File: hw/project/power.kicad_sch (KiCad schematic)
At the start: 27 parts, among them Q1 MOSFET, N-CH, SINGLE, 120A, 6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, Q2 MOSFET, N-CH, SINGLE, 120A, 6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, U3 LM74502DDFR, U4 LMR51610XDBVR

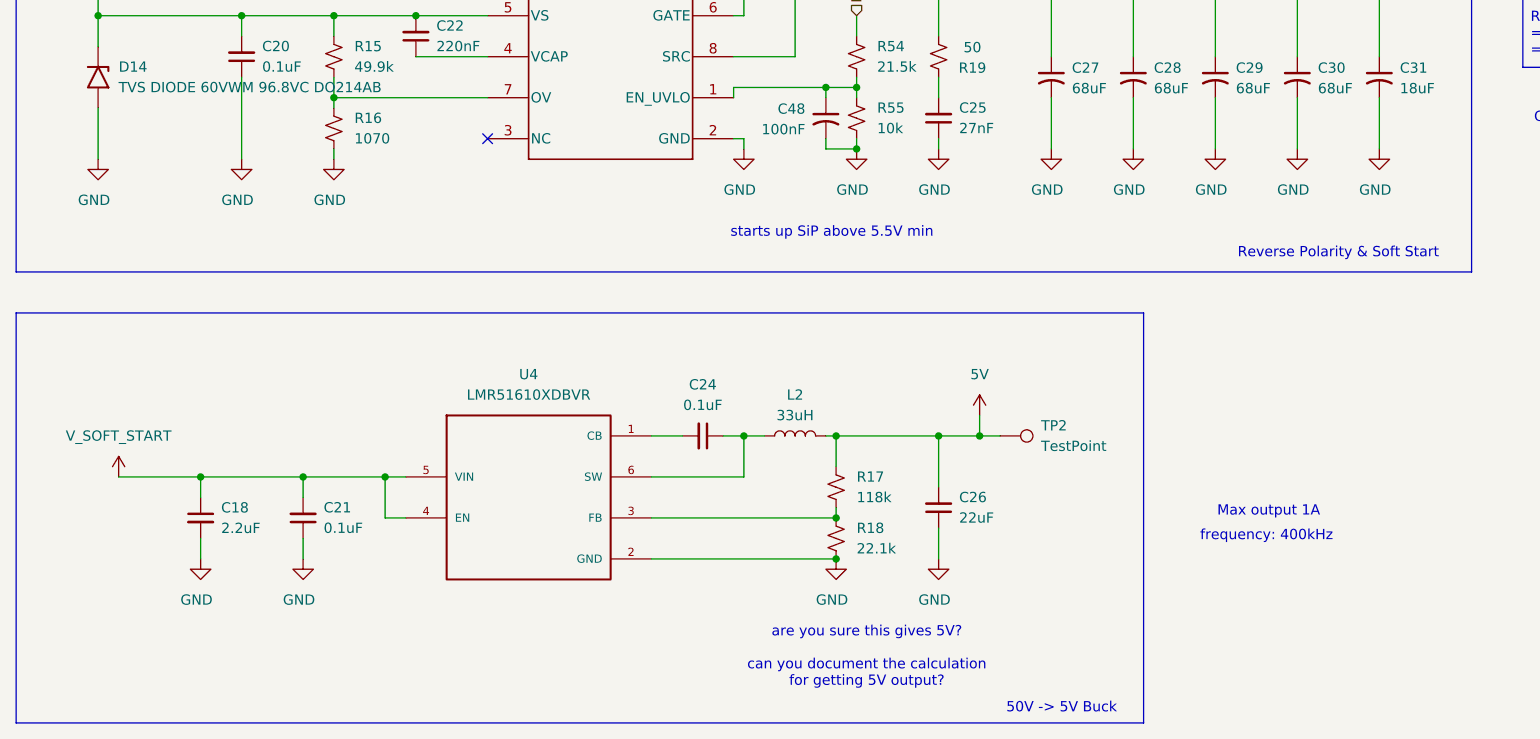
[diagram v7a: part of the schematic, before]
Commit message: Change relevant GND symbols to PGND
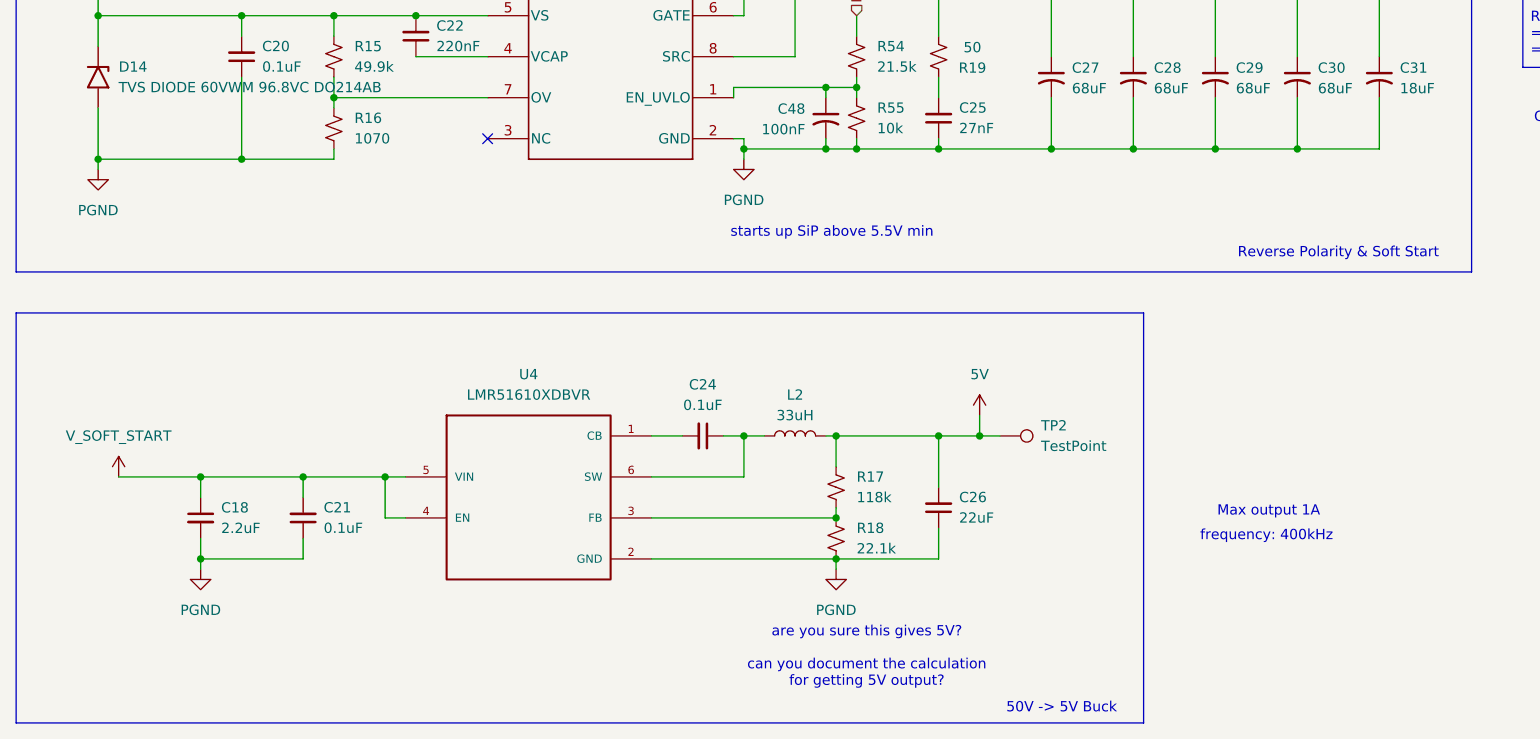
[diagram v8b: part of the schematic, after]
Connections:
- net GND renamed PGND
